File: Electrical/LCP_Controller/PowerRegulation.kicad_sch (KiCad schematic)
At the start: 21 parts, among them Q12 MMBT2222AL, Q13 TSM500P02CX RFG, U3 LMR50410

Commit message: Hardware Revision : v0.3
1. modified schematic design, removed unnecessary test points.
2. pcb layout 2x8 Inches allowance dimension, layout is in progress
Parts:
- removed TP22: 5002, TestPoint:TestPoint_Keystone_5000-5004_Miniature, symbol Connector:TestPoint
- removed TP23: 5004, TestPoint:TestPoint_Keystone_5000-5004_Miniature, symbol Connector:TestPoint
- added TP3: GND, TestPoint:TestPoint_Keystone_5000-5004_Miniature, symbol Connector:TestPoint
- TP1: renamed from TP8; value 5000 -> VIN
- TP2: renamed from TP24; value 5000 -> 3V3
- renumbered C5 to C2, C7 to C3, C6 to C4, C8 to C5, C9 to C6, C10 to C7, Q13 to Q1, Q12 to Q2, R3 to R2, R4 to R3, R30 to R4, R29 to R5, R31 to R6, R28 to R7, R32 to R8, U3 to U1
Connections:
- net GND: now also TP3.1

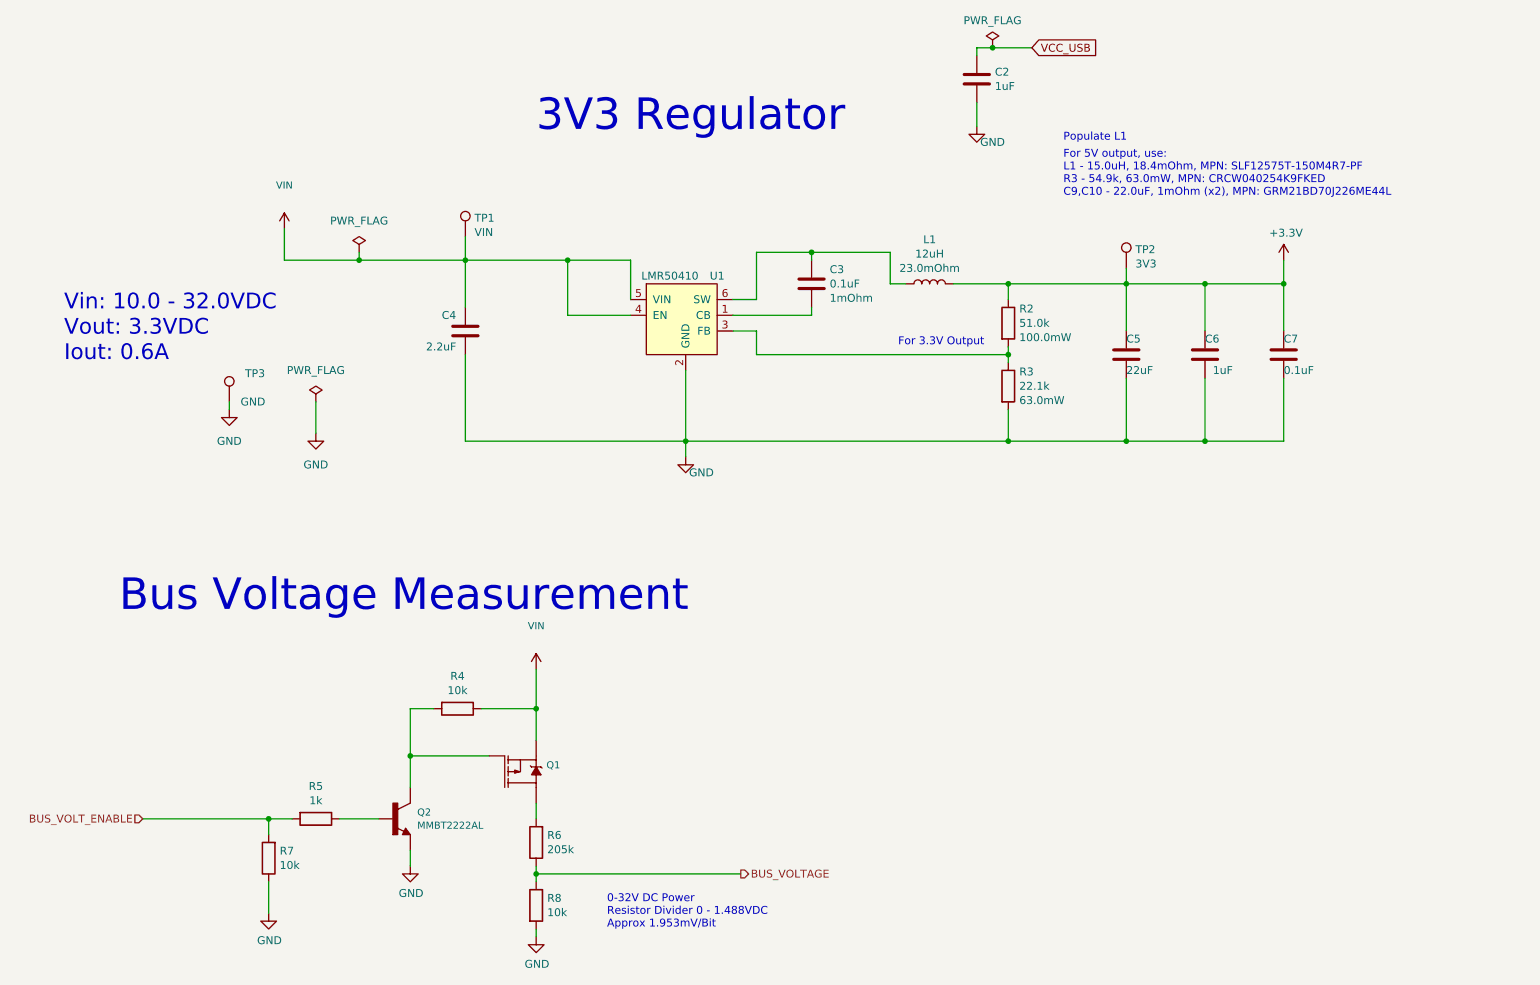
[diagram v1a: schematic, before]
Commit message: Hw Rev : 0.3v
changed buck-coverter LMR50410XDBVR to BD9G102G-LB, added schotty diode.
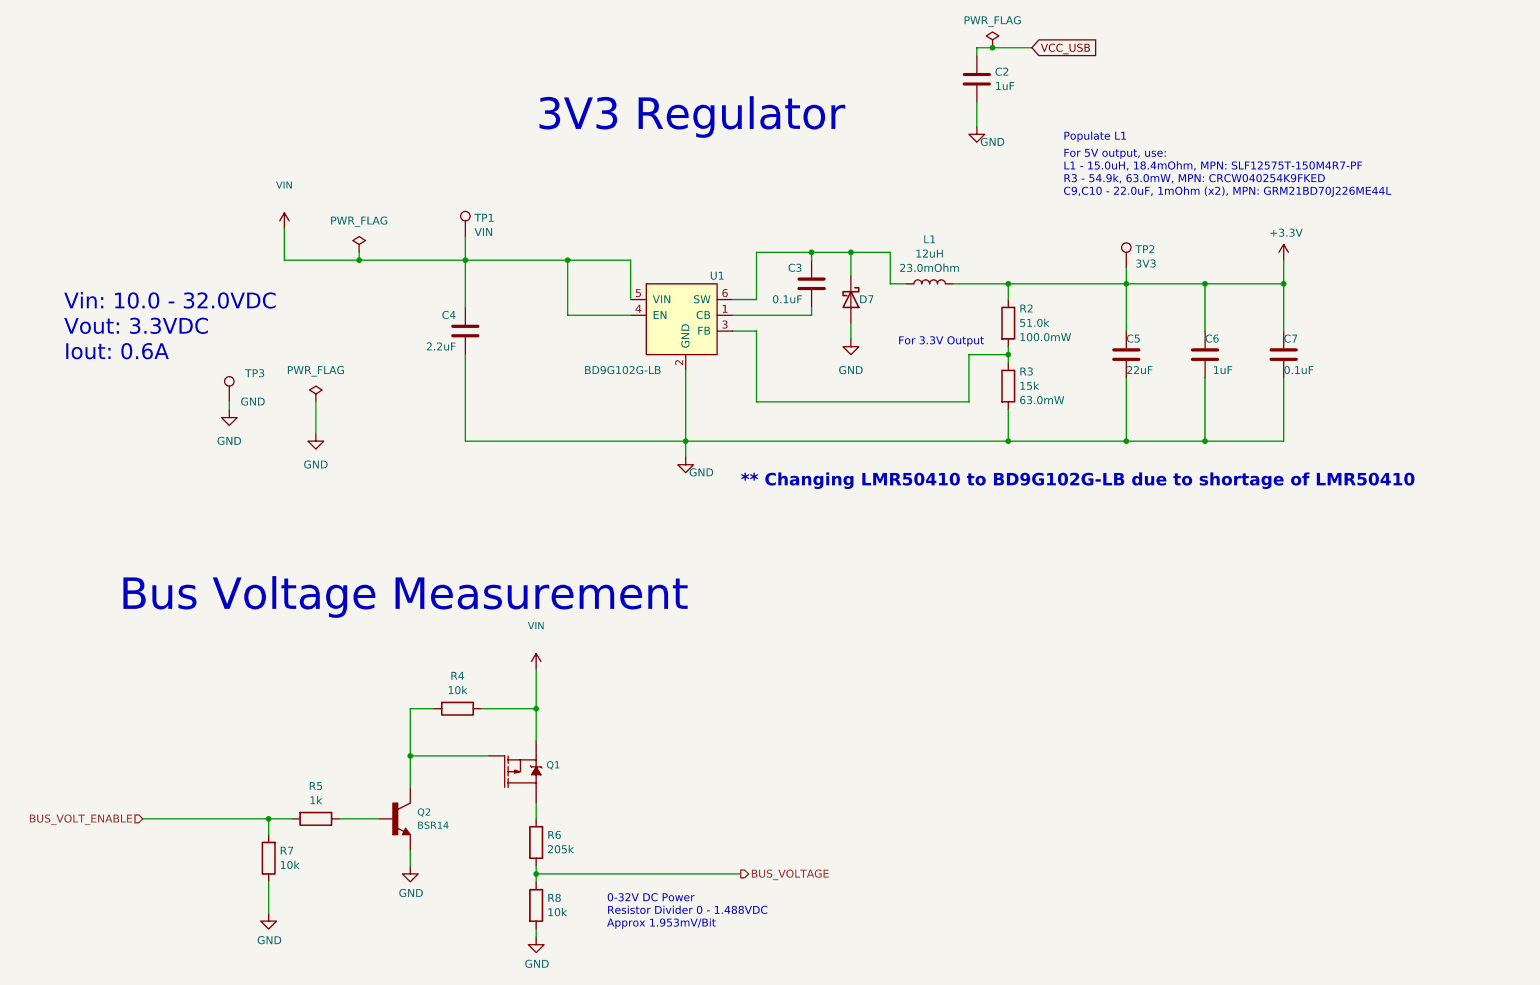
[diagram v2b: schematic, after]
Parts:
- added D7: RB400VAM-50TR, Diode_SMD:D_SOD-323, symbol Device:D_Schottky
- C4: footprint Capacitor_SMD:C_0603_1608Metric -> Capacitor_SMD:C_0805_2012Metric; ESR 5.22mOhm -> (none); MPN C1608X5R1H105K080AB -> CL21A225KB9LNNC
- C5: ESR 1mOhm -> (none); MPN CM21X7T226M06AT -> CL21A226MPQNNNE
- C6: MPN CM21X7T226M06AT -> CL21B105KOFNNNG
- C7: footprint Capacitor_SMD:C_0805_2012Metric -> Capacitor_SMD:C_0603_1608Metric; MPN CM21X7T226M06AT -> GCM188R71H104KA57D
- Q2: value MMBT2222AL -> BSR14; Field4 TRANS-08049 -> P4673145; MPN MMBT2222ALT3G -> BSR14
- R3: value 22.1k -> 15k
- R6: MPN RR1220P-2053-D-M -> RR1220P-2053-D-M
- U1: value LMR50410 -> BD9G102G-LB; MPN LMR50410XDBVR -> BD9G102G-LB
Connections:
- net GND: now also D7.2 (A)
- net at C3.1, L1.1, U1.6 (SW): now also D7.1 (K)
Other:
- note added: "** Changing LMR50410 to BD9G102G-LB due to shortage of LMR50410"

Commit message: Hw Rev : 0.3v updated
changed TRS3122ERGER to TRS3122ERGET due to shortage of part.
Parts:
- D7: footprint Diode_SMD:D_SOD-323 -> Diode_SMD:D_SOD-323F; Spice_Model (none) -> RB400VAM-50TR; Spice_Netlist_Enabled (none) -> Y; Spice_Primitive (none) -> D
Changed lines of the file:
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@@
       (effects (font (size 1.27 1.27)) hide)
     )
-    (property "Footprint" "Diode_SMD:D_SOD-323" (id 2) (at 168.91 81.28 0)
+    (property "Footprint" "Diode_SMD:D_SOD-323F" (id 2) (at 168.91 81.28 0)
       (effects (font (size 1.27 1.27)) hide)
     )
@@
       (effects (font (size 1.27 1.27)) hide)
     )
+    (property "Spice_Primitive" "D" (id 5) (at 168.91 81.28 0)
+      (effects (font (size 1.27 1.27)) hide)
+    )
+    (property "Spice_Model" "RB400VAM-50TR" (id 6) (at 168.91 81.28 0)
+      (effects (font (size 1.27 1.27)) hide)
+    )
+    (property "Spice_Netlist_Enabled" "Y" (id 7) (at 168.91 81.28 0)
+      (effects (font (size 1.27 1.27)) hide)
+    )

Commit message: Hw Rev : 0.3v , update
changed package type D_SOD-323 to D_TUMD2 for D4,D7
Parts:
- D7: footprint Diode_SMD:D_SOD-323F -> Diode_SMD:D_TUMD2
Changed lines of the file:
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@@
       (effects (font (size 1.27 1.27)) hide)
     )
-    (property "Footprint" "Diode_SMD:D_SOD-323F" (id 2) (at 168.91 81.28 0)
+    (property "Footprint" "Diode_SMD:D_TUMD2" (id 2) (at 168.91 81.28 0)
       (effects (font (size 1.27 1.27)) hide)
     )

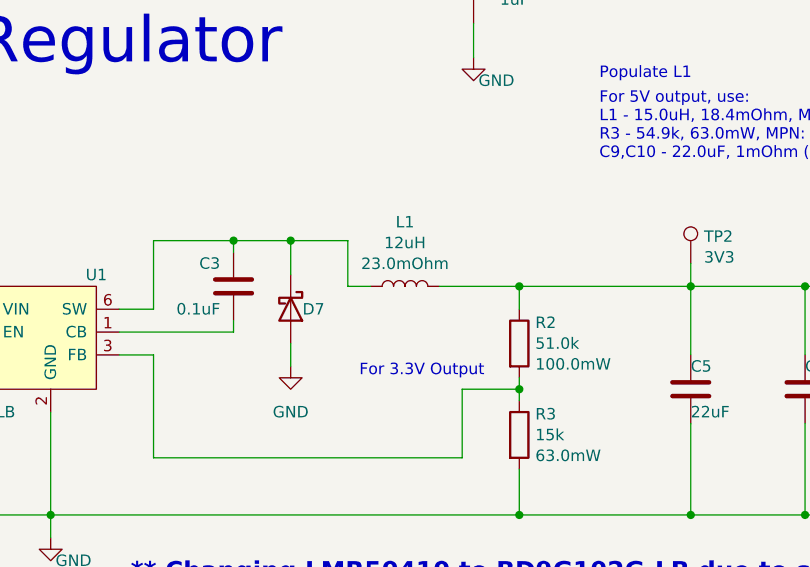
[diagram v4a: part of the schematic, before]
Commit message: Removed RF Switch
Deleted the RF Switch.

GPS Signal is routed to J17 and Iridium to J18.
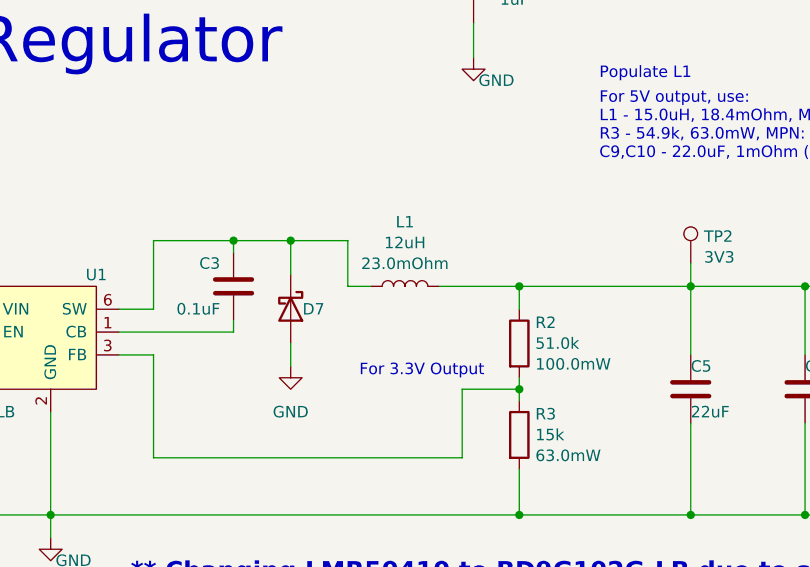
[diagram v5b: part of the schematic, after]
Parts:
- D7: Spice_Model RB400VAM-50TR -> (none); Spice_Netlist_Enabled Y -> (none); Spice_Primitive D -> (none)
